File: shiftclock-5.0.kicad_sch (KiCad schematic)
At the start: 37 parts, among them J1 USB_C_Receptacle_USB2.0_16P, SW1 SW1, SW2 SW2, SW3 SW3 / BOOT, SW4 RotaryEncoder_Switch, SW5 RESET, U1 CC56-12SURKWA, U2 CC56-12SURKWA, U3 MAX7219, U5 CH340C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

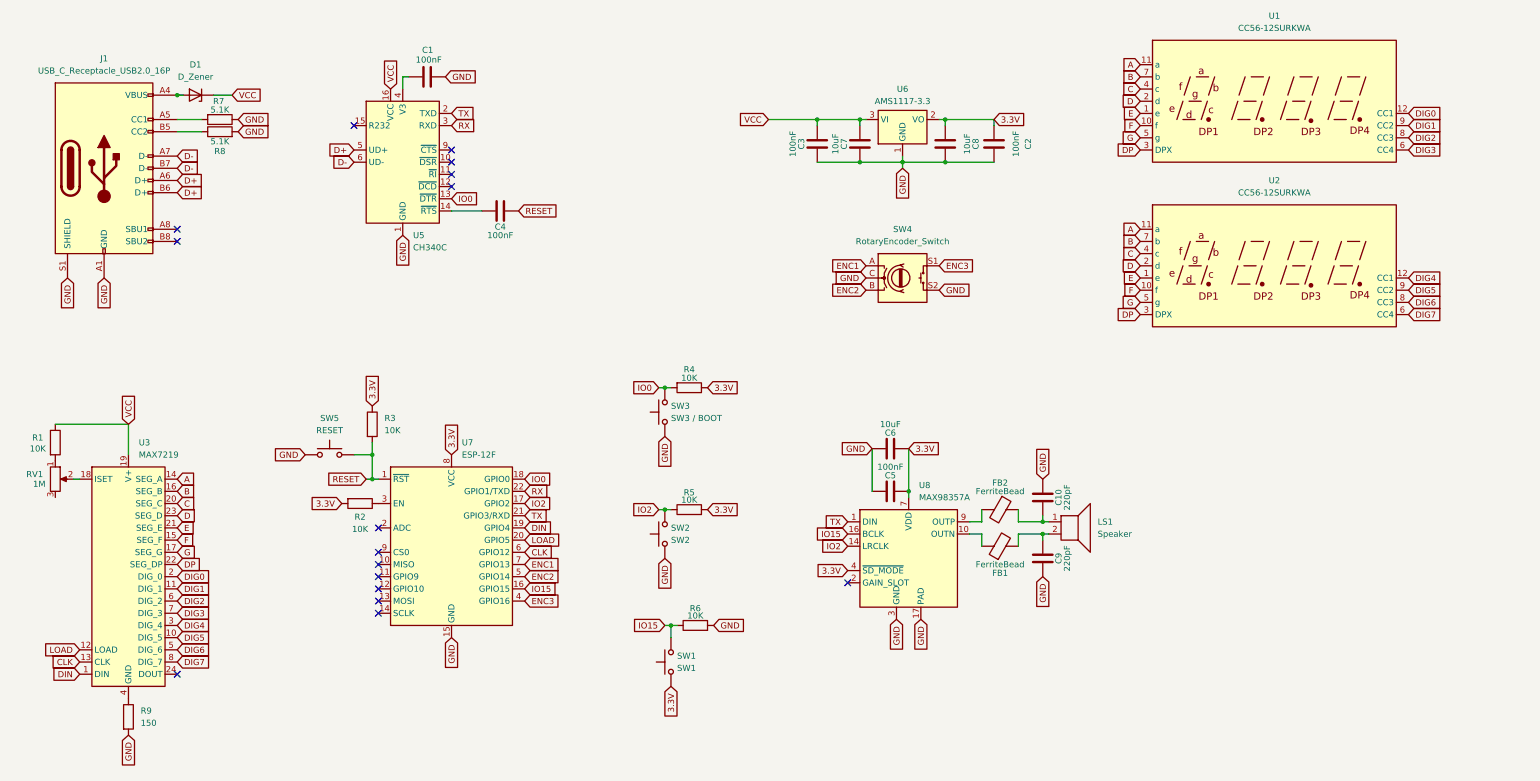
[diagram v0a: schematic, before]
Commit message: Rework Schematic and Begin Layout Connections
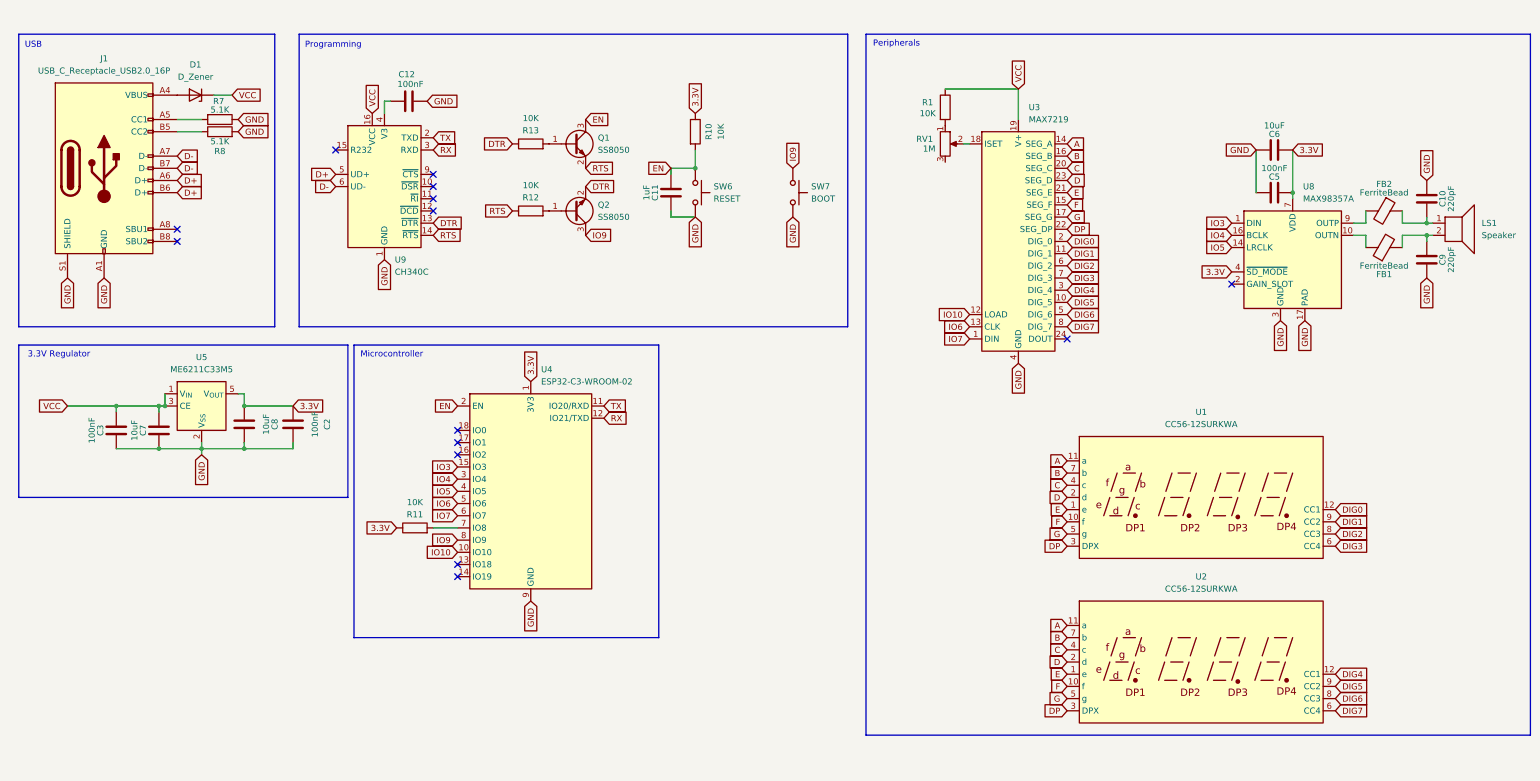
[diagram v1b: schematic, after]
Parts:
- removed C1, C4: 100nF, Capacitor_SMD:C_1206_3216Metric_Pad1.33x1.80mm_HandSolder, symbol Device:C
- removed R2, R3, R4, R5, R6: 10K, Resistor_SMD:R_1206_3216Metric_Pad1.30x1.75mm_HandSolder, symbol Device:R
- removed R9: 150, Resistor_SMD:R_1206_3216Metric_Pad1.30x1.75mm_HandSolder, symbol Device:R
- removed SW1: SW1, Button_Switch_THT:SW_PUSH_6mm_H5mm, symbol Switch:SW_Push
- removed SW2: SW2, Button_Switch_THT:SW_PUSH_6mm_H5mm, symbol Switch:SW_Push
- removed SW3: SW3 / BOOT, Button_Switch_THT:SW_PUSH_6mm_H5mm, symbol Switch:SW_Push
- removed SW4: RotaryEncoder_Switch, Rotary_Encoder:RotaryEncoder_Alps_EC12E-Switch_Vertical_H20mm_CircularMountingHoles, symbol Device:RotaryEncoder_Switch
- removed SW5: RESET, Button_Switch_SMD:SW_Tactile_SPST_NO_Straight_CK_PTS636Sx25SMTRLFS, symbol Switch:SW_Push
- removed U5: CH340C, Package_SO:SOIC-16_3.9x9.9mm_P1.27mm, symbol Interface_USB:CH340C
- removed U6: AMS1117-3.3, Package_TO_SOT_SMD:SOT-223-3_TabPin2, symbol Regulator_Linear:AMS1117-3.3
- removed U7: ESP-12F, RF_Module:ESP-12E, symbol RF_Module:ESP-12F
- added C11: 1uF, Capacitor_SMD:C_1206_3216Metric_Pad1.33x1.80mm_HandSolder, symbol Device:C
- added C12: 100nF, Capacitor_SMD:C_1206_3216Metric_Pad1.33x1.80mm_HandSolder, symbol Device:C
- added Q1, Q2: SS8050, Package_TO_SOT_SMD:SOT-23, symbol Transistor_BJT:SS8050
- added R10, R11, R12, R13: 10K, Resistor_SMD:R_1206_3216Metric_Pad1.30x1.75mm_HandSolder, symbol Device:R
- added SW6: RESET, Button_Switch_SMD:SW_Tactile_SPST_NO_Straight_CK_PTS636Sx25SMTRLFS, symbol Switch:SW_Push
- added SW7: BOOT, Button_Switch_SMD:SW_Tactile_SPST_NO_Straight_CK_PTS636Sx25SMTRLFS, symbol Switch:SW_Push
- added U4: ESP32-C3-WROOM-02, RF_Module:ESP32-C3-WROOM-02, symbol RF_Module:ESP32-C3-WROOM-02
- added U5: ME6211C33M5, Package_TO_SOT_SMD:SOT-23-5, symbol Regulator_Linear:ME6211C33M5
- added U9: CH340C, Package_SO:SOIC-16_3.9x9.9mm_P1.27mm, symbol Interface_USB:CH340C
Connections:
- net 3.3V: now also R10.1, R11.1, U4.1 (3V3), U5.5 (V_{OUT})
- net D+: now also U9.5 (UD+)
- net D-: now also U9.6 (UD-)
- net GND: now also U3.4 (GND), U3.9 (GND), C11.2, C12.2, SW6.2, SW7.2, U4.19 (GND), U4.9 (GND), U5.2 (V_{SS}), U9.1 (GND)
- net RX: now also U4.12 (IO21/TXD), U9.3 (RXD)
- net TX: now also U4.11 (IO20/RXD), U9.2 (TXD); no longer U8.1 (DIN)
- net VCC: now also U5.1 (V_{IN}), U5.3 (CE), U9.16 (VCC)
- net CLK renamed IO6
- net IO6: now also U4.5 (IO6)
- net DIN renamed IO7
- net IO7: now also U4.6 (IO7)
- net IO15 renamed IO4
- net IO4: now also U4.3 (IO4)
- net IO2 renamed IO5
- net IO5: now also U4.4 (IO5)
- net LOAD renamed IO10
- net IO10: now also U4.10 (IO10)
- new net: C12.1, U9.4 (V3)
- new net: R11.2, U4.7 (IO8)
- new net: Q2.1 (B), R12.2
- new net: Q1.1 (B), R13.2
- new net DTR: Q2.2 (E), R13.1, U9.13 (~{DTR})
- new net EN: C11.1, Q1.3 (C), R10.2, SW6.1, U4.2 (EN)
- new net IO3: U4.15 (IO3), U8.1 (DIN)
- new net IO9: Q2.3 (C), SW7.1, U4.8 (IO9)
- new net RTS: Q1.2 (E), R12.1, U9.14 (~{RTS})
- no-connect marks 16 -> 14
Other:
- note added: "3.3V Regulator"
- note added: "Microcontroller"
- note added: "Peripherals"
- note added: "Programming"
- note added: "USB"
- moved on the sheet: C10, C2, C3, C5, C6, C7, C8, C9, FB1, FB2, LS1, R1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

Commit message: Add Netlist
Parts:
- added R2: 10K, Resistor_SMD:R_1206_3216Metric_Pad1.30x1.75mm_HandSolder, symbol Device:R
- added TP1, TP2, TP3, TP4, TP5, TP6, TP7: TestPoint, TestPoint:TestPoint_Pad_2.0x2.0mm, symbol Connector:TestPoint
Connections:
- net 3.3V: now also R2.1, TP2.1
- net DTR: now also TP6.1
- net GND: now also TP3.1
- net IO9: now also R2.2
- net RTS: now also TP7.1
- net RX: now also TP5.1
- net TX: now also TP4.1
- net VCC: now also TP1.1
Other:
- note added: "Test Points"
